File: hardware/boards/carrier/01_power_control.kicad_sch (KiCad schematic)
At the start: 42 parts, among them Q1 IPB020N10N5LF, Q2 2N7002, Q3 2N7002, U3 LMX5069MS, U4 INA237AIDGSR, U5 TCAN3413DR

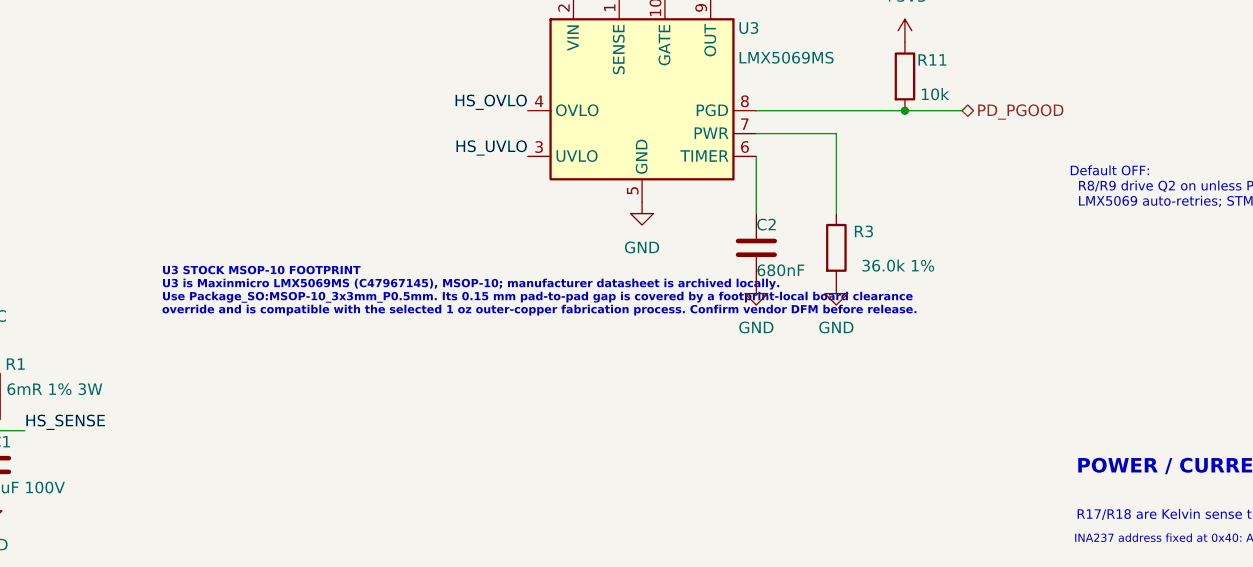
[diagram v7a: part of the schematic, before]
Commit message: restore carrier U3 clearance footprint
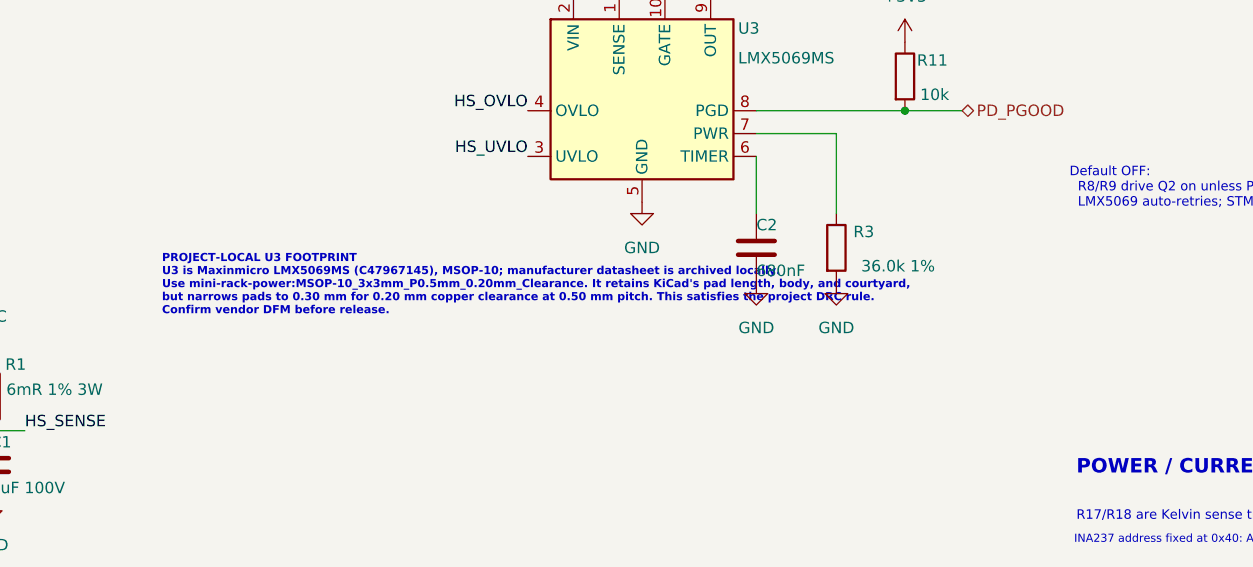
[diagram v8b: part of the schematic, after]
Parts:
- U3: footprint Package_SO:MSOP-10_3x3mm_P0.5mm -> mini-rack-power:MSOP-10_3x3mm_P0.5mm_0.20mm_Clearance
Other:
- note added: "PROJECT-LOCAL U3 FOOTPRINT U3 is Maxinmicro LMX5069MS (C47967145), MSOP-10; manufacturer datasheet is archived locally. Use mini-rack-power:MSOP-10_3x3mm_P0.5mm_0.20mm_Clearance. It retains KiCad's pad length, body, and courtyard, but narrows pads to 0.30 mm for 0.20 mm copper clearance at 0.50 mm pitch. This satisfies the project DRC rule. Confirm vendor DFM before release."
- note removed: "U3 STOCK MSOP-10 FOOTPRINT U3 is Maxinmicro LMX5069MS (C47967145), MSOP-10; manufacturer datasheet is archived locally. Use Package_SO:MSOP-10_3x3mm_P0.5mm. Its 0.15 mm pad-to-pad gap is covered by a footprint-local board clearance override and is compatible with the selected 1 oz outer-copper fabrication process. Confirm vendor DFM before release."
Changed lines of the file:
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@@
 		)
 	)
-	(text "U3 STOCK MSOP-10 FOOTPRINT\nU3 is Maxinmicro LMX5069MS (C47967145), MSOP-10; manufacturer datasheet is archived locally.\nUse Package_SO:MSOP-10_3x3mm_P0.5mm. Its 0.15 mm pad-to-pad gap is covered by a footprint-local board clearance\noverride and is compatible with the selected 1 oz outer-copper fabrication process. Confirm vendor DFM before release."
+	(text "PROJECT-LOCAL U3 FOOTPRINT\nU3 is Maxinmicro LMX5069MS (C47967145), MSOP-10; manufacturer datasheet is archived locally.\nUse mini-rack-power:MSOP-10_3x3mm_P0.5mm_0.20mm_Clearance. It retains KiCad's pad length, body, and courtyard,\nbut narrows pads to 0.30 mm for 0.20 mm copper clearance at 0.50 mm pitch. This satisfies the project DRC rule.\nConfirm vendor DFM before release."
 		(exclude_from_sim no)
 		(at 93.98 76.2 0)
@@
 			)
 		)
-		(property "Footprint" "Package_SO:MSOP-10_3x3mm_P0.5mm"
+		(property "Footprint" "mini-rack-power:MSOP-10_3x3mm_P0.5mm_0.20mm_Clearance"
 			(at 148.59 28.956 0)
 			(hide yes)
